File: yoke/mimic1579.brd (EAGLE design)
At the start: 165.1 x 114.3 mm, 77 parts, among them J1 44PINEDGE, P2 2K, P3 2K, Q1 2N3904, Q13 2N3904, Q14 2N3904, Q15 2N3906, Q16 2N3904, Q2 2N3906, Q3 2N3906, Q4 2N3906, Q5 2N3904, Q6 2N3904, Q7 2N3906, Q8 2N3904, Q9 2N3904

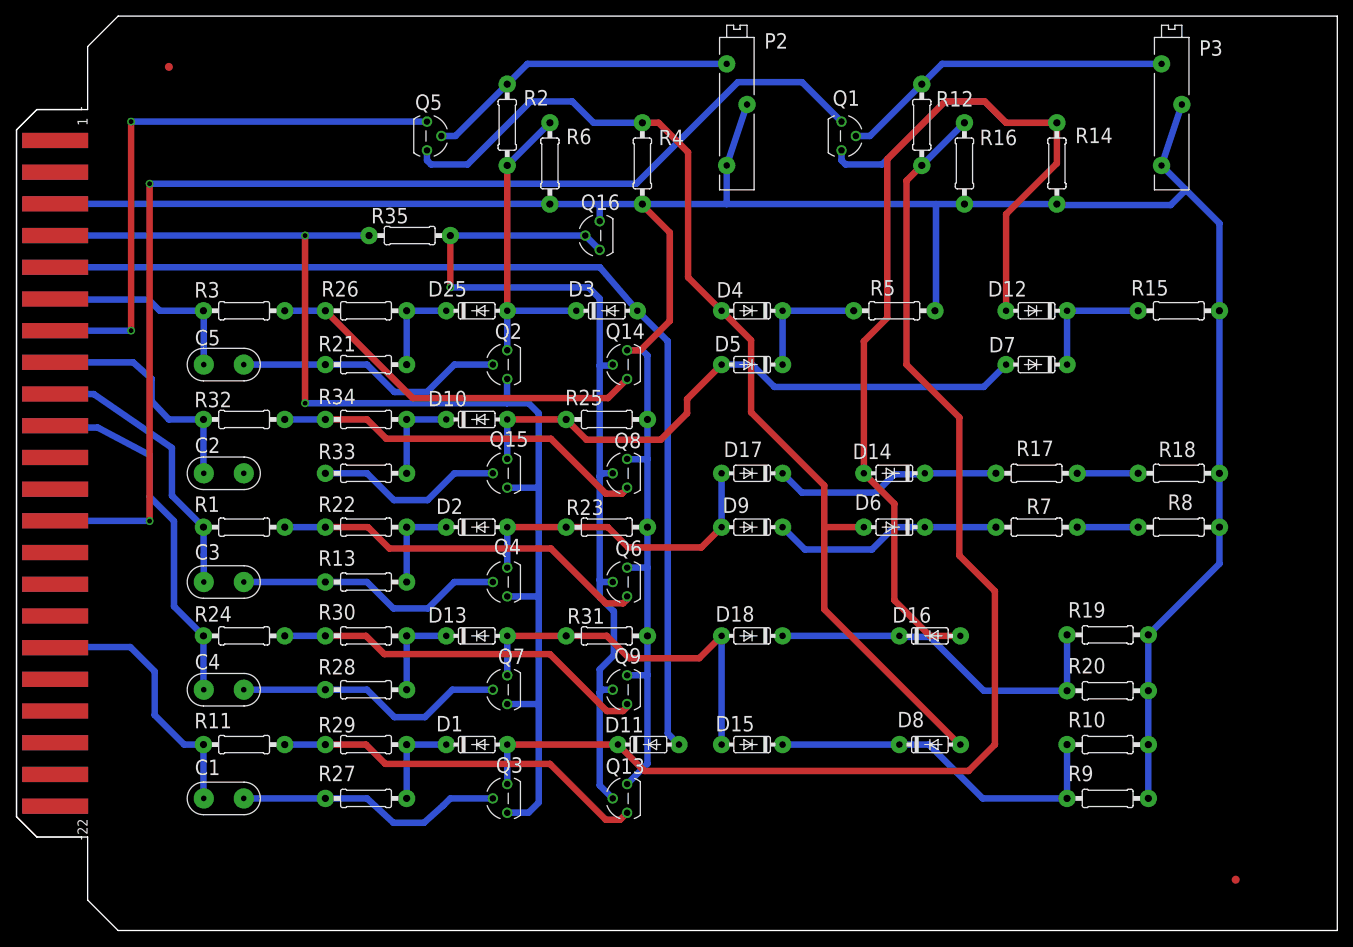
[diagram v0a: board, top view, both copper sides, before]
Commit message: preamplifier card being routed
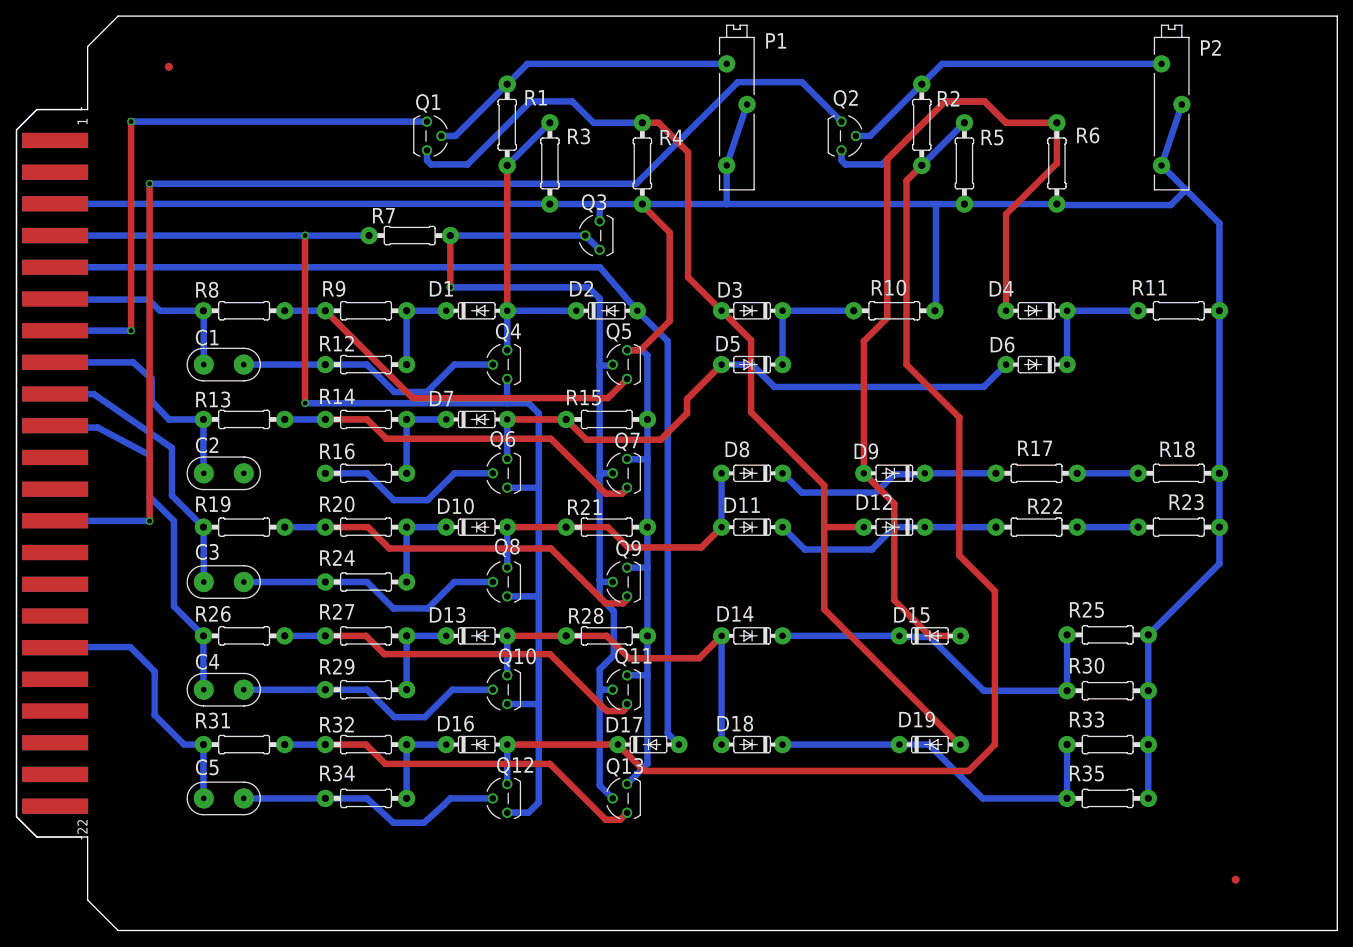
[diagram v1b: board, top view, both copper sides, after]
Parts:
- removed D25: 1N4148, keiths:DO35-7
- removed P3: 2K, keiths:3006P
- removed Q14, Q16: 2N3904, keiths:TO92
- removed Q15: 2N3906, keiths:TO92
- added D19: 1N4148, keiths:DO35-7
- added P1: 2K, keiths:3006P
- added Q10, Q12: 2N3906, keiths:TO92
- added Q11: 2N3904, keiths:TO92
- D11, D3: value BAT48 -> 1N4148
- D17, D2: value 1N4148 -> BAT48
- Q2, Q3, Q7: value 2N3906 -> 2N3904
- Q6, Q8: value 2N3904 -> 2N3906
- R1: value 4.75K -> 4.7K
- R10: value 1.5K -> 10K
- R11: value 4.75K -> 10K
- R12: value 4.7K -> 475
- R13, R26: value 475 -> 4.75K
- R14: value 18K -> 475
- R16, R20, R9: value 1.5K -> 475
- R19: value 1.5K -> 4.75K
- R21, R28: value 475 -> 10K
- R22: value 475 -> 1K
- R23: value 10K -> 1K
- R24, R32: value 4.75K -> 475
- R25, R5: value 10K -> 1.5K
- R3: value 4.75K -> 1.5K
- R30, R33: value 475 -> 1.5K
- R31: value 10K -> 4.75K
- R35: value 18K -> 1.5K
- R6: value 1.5K -> 18K
- R7: value 1K -> 18K
- R8: value 1K -> 4.75K
- moved U$1 167.6 mm to (19.1, 108.0)
- moved U$2 167.6 mm to (152.4, 6.35)
- moved R11 128.8 mm to (145.3, 77.5)
- moved R8 119.9 mm to (28.4, 77.5)
- moved R35 112.1 mm to (136.4, 16.5), turned to 0 degrees
- moved R9 111.0 mm to (43.7, 77.5), turned to 180 degrees
- moved R19 108.8 mm to (28.4, 50.4)
- moved R33 98.7 mm to (136.4, 23.2)
- moved R20 94.9 mm to (43.7, 50.4), turned to 180 degrees
- moved R30 93.0 mm to (136.4, 30.0), turned to 0 degrees
- moved R14 92.1 mm to (43.7, 63.9), turned to 180 degrees
- moved R7 86.4 mm to (49.1, 86.9), turned to 180 degrees
- moved R16 84.2 mm to (43.7, 57.1), turned to 0 degrees
- moved R22 83.8 mm to (127.5, 50.4), turned to 0 degrees
- moved R12 75.7 mm to (43.7, 70.7), turned to 0 degrees
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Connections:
- net -10V: now also D17.A, D2.A; no longer D11.A, D3.A
- net -15V: now also P1.1, P1.2, Q11.1, Q3.1, Q5.1, Q7.1, R11.2, R15.1, R21.1, R23.2, R25.2, R28.1, R3.2, R30.2, R33.2, R35.2; no longer P3.1, P3.2, Q14.1, Q16.1, Q6.1, Q8.1, R14.2, R15.2, R16.2, R19.2, R20.2, R23.1, R25.1, R31.1, R8.2, R9.2
- net F_IN: now also C1.1, R8.1; no longer C5.1, R3.1
- net GND: now also Q10.3, Q12.3, Q6.3, Q8.3, R7.2; no longer Q15.3, Q2.3, Q3.3, Q7.3, R35.2
- net H_OUT: now also Q1.3; no longer Q5.3
- net J_IN: now also R13.1; no longer R32.1
- net K_IN: now also R19.1; no longer R1.1
- net L_IN: now also R26.1; no longer R24.1
- net N$1: now also C1.2, Q4.2, R12.1; no longer C5.2, Q2.2, R21.1
- net N$10: now also D11.C, D12.C, R22.1; no longer D6.C, D9.C, R7.1
- net N$11: now also D18.C, D19.C, R33.1, R35.1; no longer D15.C, D8.C, R10.1, R9.1
- net N$12: now also D10.C, R20.1, R24.2; no longer D2.C, R13.2, R22.1
- net N$13: now also Q10.2, R29.1; no longer Q7.2, R28.1
- net N$14: now also C5.2, Q12.2, R34.1; no longer C1.2, Q3.2, R27.1
- net N$15: now also R31.2, R32.2; no longer R11.2, R29.2
- net N$16: now also P2.3, Q2.2, R2.2; no longer P3.3, Q1.2, R12.2
- net N$17: now also D15.A, D4.A, D9.A, Q2.1, R6.1; no longer D12.A, D14.A, D16.A, Q1.1, R14.1
- net N$18: now also D4.C, D6.C, R11.1; no longer D12.C, D7.C, R15.1
- net N$19: now also D8.C, D9.C; no longer D14.C, D17.C
- net N$2: now also Q5.3, R8.2, R9.2; no longer Q14.3, R26.2, R3.2
- net N$21: now also D14.C, D15.C, R25.1, R30.1; no longer D16.C, D18.C, R19.1, R20.1
- net N$22: now also Q11.3, R26.2, R27.2; no longer Q9.3, R24.2, R30.2
- net N$23: now also R27.1, R29.2; no longer R28.2, R30.1
- net N$25: now also D16.C, R32.1, R34.2; no longer D1.C, R27.2, R29.1
- net N$3: now also Q8.2, R24.1; no longer Q4.2, R13.1
- net N$30: now also Q6.2, R16.1; no longer Q15.2, R33.1
- net N$31: now also Q7.3, R13.2, R14.2; no longer Q8.3, R32.2, R34.2
- net N$32: now also D7.C, R14.1, R16.2; no longer D10.C, R33.2, R34.1
- net N$33: now also Q11.2, Q3.2, Q3.3, Q5.2, Q7.2, R7.1; no longer Q14.2, Q16.2, Q16.3, Q6.2, Q8.2, R35.1
- net N$4: now also P1.3, Q1.2, R1.2; no longer P2.3, Q5.2, R2.2
- net N$5: now also D12.A, D19.A, D3.A, Q1.1; no longer D4.A, D6.A, D8.A, Q5.1
- net N$6: now also D3.C, R10.1; no longer D4.C, R5.1
- net N$7: now also R22.2, R23.1; no longer R7.2, R8.1
- net N$8: now also Q9.3, R19.2, R20.2; no longer Q6.3, R1.2, R22.2
- net N$9: now also D1.C, R12.2, R9.1; no longer D25.C, R21.2, R26.1
- net P_OUT: now also Q2.3; no longer Q1.3
- net U_IN: now also C5.1, R31.1; no longer C1.1, R11.1
- net VREF: now also D1.A, D2.C, Q4.1, R1.1, R3.1; no longer D25.A, D3.C, Q2.1, R2.1, R6.1
- net VREF1: now also D10.A, D11.A, D8.A, Q8.1, R21.2; no longer D17.A, D2.A, D9.A, Q4.1, R23.2
- net VREF2: now also D14.A, Q10.1, R28.2; no longer D15.A, Q7.1, R31.2
- net VREF3: now also D6.A, Q6.1, R15.2; no longer D10.A, Q15.1, R25.2
- net VREF5: now also D16.A, D17.C, Q12.1, R2.1, R5.1; no longer D1.A, D11.C, Q3.1, R12.1, R16.1

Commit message: added logo
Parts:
- moved U$1 17.8 mm to (36.8, 108.0)
- moved R25 11.1 mm to (145.3, 43.6)
- moved R30 11.1 mm to (145.3, 36.6)
- moved R33 11.1 mm to (145.3, 29.8)
- moved R35 11.1 mm to (145.3, 23.1)
- moved D5 4.70 mm to (91.9, 66.0)
- moved D11 2.54 mm to (91.9, 47.9)
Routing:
- net -15V: track 352.5 -> 342.2 mm
- net N$21: track 45.4 -> 54.3 mm
- net N$11: track 45.1 -> 53.9 mm
- net N$6: track 15.6 -> 20.3 mm
- net U_IN: track 33.6 -> 30.4 mm
- net J_IN: track 29.9 -> 28.3 mm
- net VREF1: track 40.7 -> 42.2 mm
- net L_IN: track 44.9 -> 43.7 mm
- net N$10: track 29.0 -> 27.8 mm
- net VREF3: track 75.6 -> 74.4 mm
- net K_IN: track 35.1 -> 34.3 mm
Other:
- board text added: "board type 1579 / feed forward"
